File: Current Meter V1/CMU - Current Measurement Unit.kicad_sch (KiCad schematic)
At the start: 29 parts, among them J101 I2C OLED Display Connector, U101 MCP6002-xSN, U102 A1308xLHxx-1, U103 STM32L432KCUx

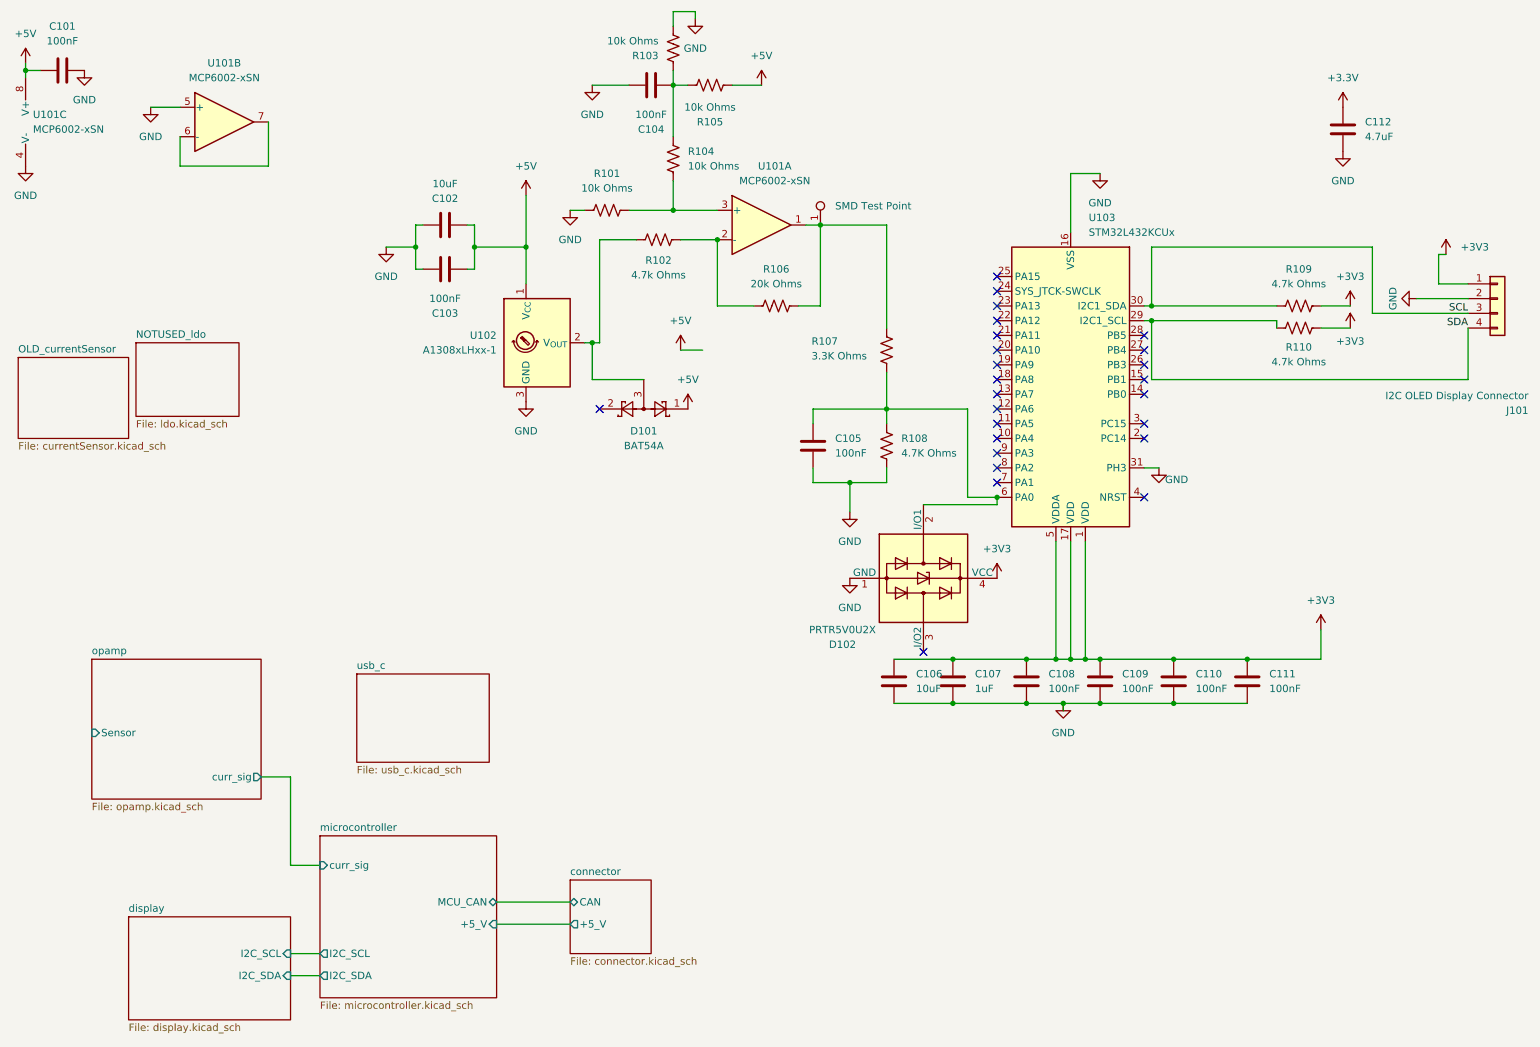
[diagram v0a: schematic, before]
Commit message: updated footprints
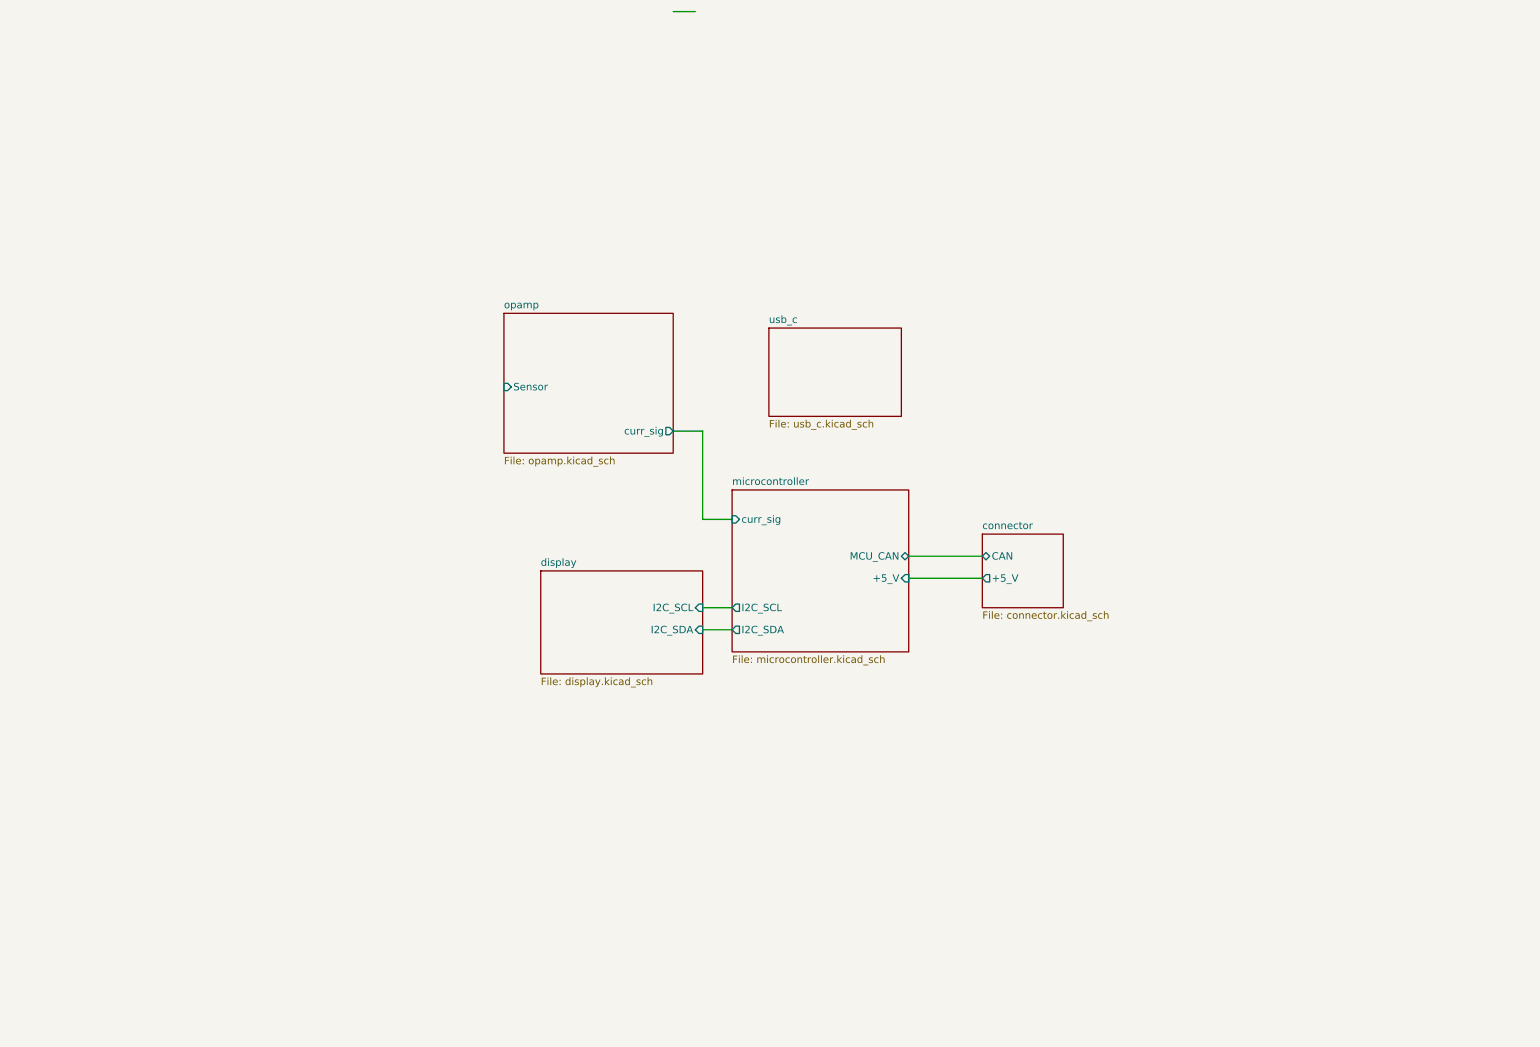
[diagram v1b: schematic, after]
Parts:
- removed C101, C103, C104, C105, C108, C109, C110, C111: 100nF, symbol Device:C
- removed C102, C106: 10uF, symbol Device:C
- removed C107: 1uF, symbol Device:C
- removed C112: 4.7uF, symbol Device:C
- removed D101: BAT54A, Package_TO_SOT_SMD:SOT-23, symbol Diode:BAT54A
- removed D102: PRTR5V0U2X, Package_TO_SOT_SMD:SOT-143, symbol Power_Protection:PRTR5V0U2X
- removed J101: I2C OLED Display Connector, symbol Connector_Generic:Conn_01x04
- removed R101, R103, R104, R105: 10k Ohms, symbol Device:R_US
- removed R102, R109, R110: 4.7k Ohms, symbol Device:R_US
- removed R106: 20k Ohms, symbol Device:R_US
- removed R107: 3.3K Ohms, symbol Device:R_US
- removed R108: 4.7K Ohms, symbol Device:R_US
- removed TP101: SMD Test Point, TestPoint:TestPoint_Keystone_5019_Miniature, symbol bfr_utilities:SMD_Test_Point
- removed U101: MCP6002-xSN, symbol Amplifier_Operational:MCP6002-xSN
- removed U102: A1308xLHxx-1, Package_TO_SOT_SMD:SOT-23W, symbol Sensor_Magnetic:A1308xLHxx-1
- removed U103: STM32L432KCUx, Package_DFN_QFN:QFN-32-1EP_5x5mm_P0.5mm_EP3.45x3.45mm, symbol MCU_ST_STM32L4:STM32L432KCUx
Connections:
- no-connect marks 25 -> 0
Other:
- removed sheet NOTUSED_ldo
- removed sheet OLD_currentSensor

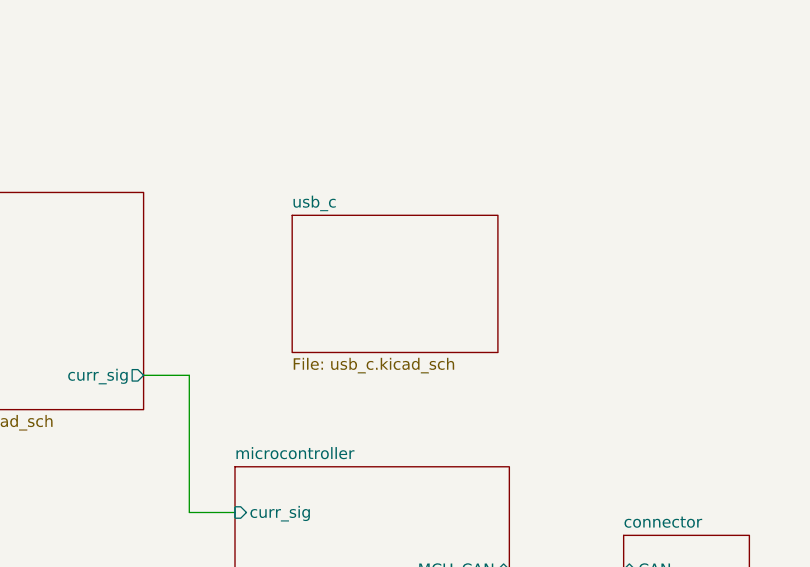
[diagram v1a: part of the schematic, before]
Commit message: footprints fully updated
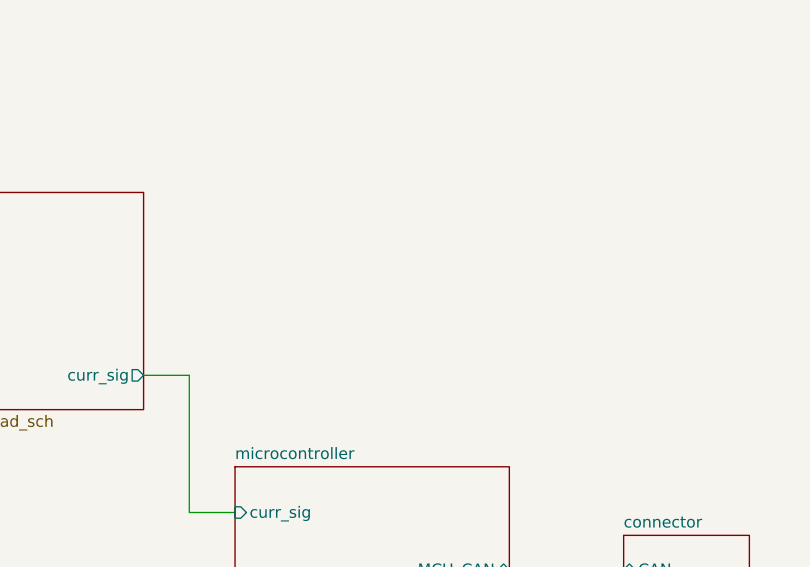
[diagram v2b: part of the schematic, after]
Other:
- removed sheet usb_c
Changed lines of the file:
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@@
-	)
-	(sheet
-		(at 147.32 69.85)
-		(size 22.86 15.24)
-		(exclude_from_sim no)
-		(in_bom yes)
-		(on_board yes)
-		(dnp no)
-		(fields_autoplaced yes)
-		(stroke
-			(width 0.1524)
-			(type solid)
-		)
-		(fill
-			(color 0 0 0 0.0000)
-		)
-		(property "Sheetname" "usb_c"
-			(at 147.32 69.1384 0)
-			(effects
-				(font
-					(size 1.27 1.27)
-				)
-				(justify left bottom)
-			)
-		)
-		(property "Sheetfile" "usb_c.kicad_sch"
-			(at 147.32 85.6746 0)
-			(effects
-				(font
-					(size 1.27 1.27)
-				)
-				(justify left top)
-			)
-		)
-		(instances
-			(project "CMU - Current Measurement Unit"
-				(path "/a2a38fd0-928e-4aba-88ec-c7bc808fdbf7"
-					(page "6")
-				)
-			)
-		)
 	)
 	(sheet

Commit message: buck converter
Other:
- added sheet buck (buck.kicad_sch)
- sheet connector ports: added +12_V; removed +5_V
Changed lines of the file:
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@@
 			)
 		)
-		(pin "+5_V" output
+		(pin "+12_V" output
 			(at 184.15 113.03 180)
 			(effects
@@
 				)
 			)
+		)
+	)
+	(sheet
+		(at 175.26 128.27)
+		(size 41.91 21.59)
+		(exclude_from_sim no)
+		(in_bom yes)
+		(on_board yes)
+		(dnp no)
+		(fields_autoplaced yes)
+		(stroke
+			(width 0.1524)
+			(type solid)
+		)
+		(fill
+			(color 0 0 0 0.0000)
+		)
+		(property "Sheetname" "buck"
+			(at 175.26 127.5584 0)
+			(effects
+				(font
+					(size 1.27 1.27)
+				)
+				(justify left bottom)
+			)
+		)
+		(property "Sheetfile" "buck.kicad_sch"
+			(at 175.26 150.4446 0)
+			(effects
+				(font
+					(size 1.27 1.27)
+				)
+				(justify left top)
+			)
+		)
+		(property "Field2" ""
+			(at 175.26 128.27 0)
+			(effects
+				(font
+					(size 1.27 1.27)
+				)
+			)
+		)
+		(pin "+5_V" output
+			(at 184.15 128.27 90)
+			(effects
+				(font
+					(size 1.27 1.27)
+				)
+				(justify right)
+			)
+		)
+		(pin "VIN" input
+			(at 217.17 142.24 0)
+			(effects
+				(font
+					(size 1.27 1.27)
+				)
+				(justify right)
+			)
+		)
+		(instances
+			(project "CMU - Current Measurement Unit"
+				(path "/a2a38fd0-928e-4aba-88ec-c7bc808fdbf7"
+					(page "6")
+				)
+			)

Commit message: layup updated
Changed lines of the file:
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@@
+	(wire
+		(pts
+			(xy 203.2 113.03) (xy 203.2 128.27)
+		)
+		(stroke
+			(width 0)
+			(type default)
+		)
+	)
 	(wire
 		(pts
@@
 	(wire
 		(pts
+			(xy 180.34 128.27) (xy 180.34 113.03)
+		)
+		(stroke
+			(width 0)
+			(type default)
+		)
+	)
+	(wire
+		(pts
+			(xy 198.12 113.03) (xy 203.2 113.03)
+		)
+		(stroke
+			(width 0)
+			(type default)
+		)
+	)
+	(wire
+		(pts
 			(xy 171.45 109.22) (xy 184.15 109.22)
 		)
@@
 	(wire
 		(pts
-			(xy 171.45 113.03) (xy 184.15 113.03)
+			(xy 171.45 113.03) (xy 180.34 113.03)
 		)
 		(stroke
@@
 		)
 		(pin "+12_V" output
-			(at 184.15 113.03 180)
-			(effects
-				(font
-					(size 1.27 1.27)
-				)
-				(justify left)
+			(at 198.12 113.03 0)
+			(effects
+				(font
+					(size 1.27 1.27)
+				)
+				(justify right)
 			)
 		)
@@
 		)
 		(pin "+5_V" output
-			(at 184.15 128.27 90)
+			(at 180.34 128.27 90)
 			(effects
 				(font
@@
 		)
 		(pin "VIN" input
-			(at 217.17 142.24 0)
-			(effects
-				(font
+			(at 203.2 128.27 90)
+			(effects
+				(font

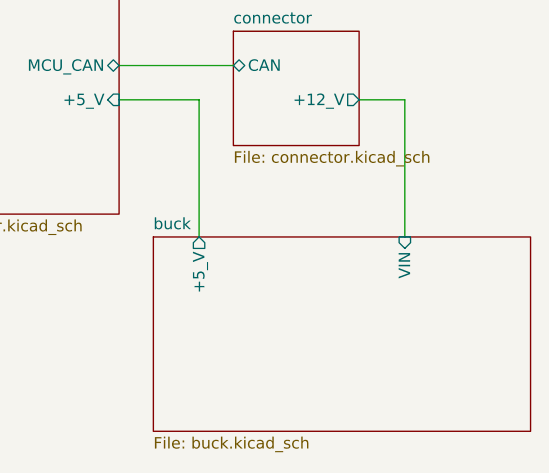
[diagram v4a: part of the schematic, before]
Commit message: updated layout
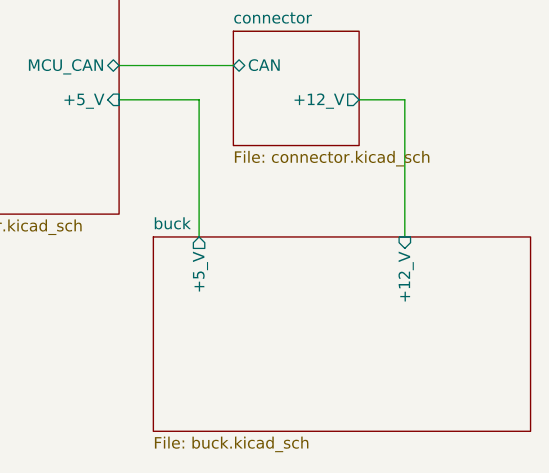
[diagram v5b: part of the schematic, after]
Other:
- sheet buck ports: added +12_V; removed VIN
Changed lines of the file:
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@@
 			)
 		)
-		(pin "VIN" input
+		(pin "+12_V" input
 			(at 203.2 128.27 90)
 			(effects

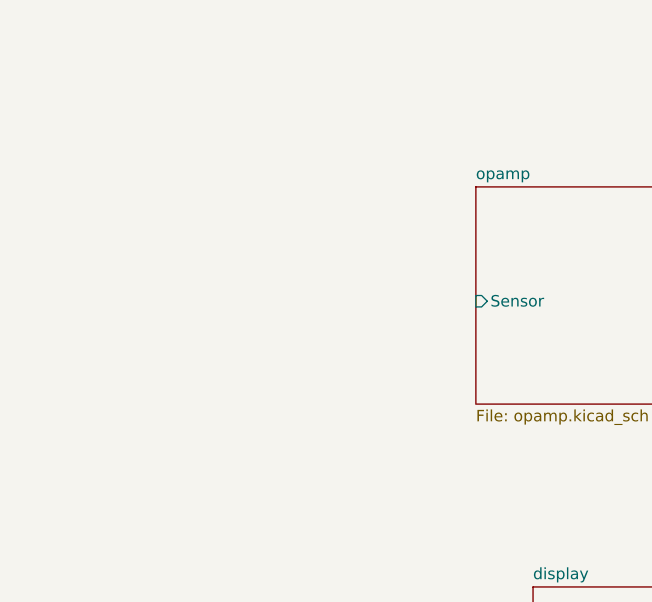
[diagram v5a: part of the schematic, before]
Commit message: added sensor connector, updated pcb layout
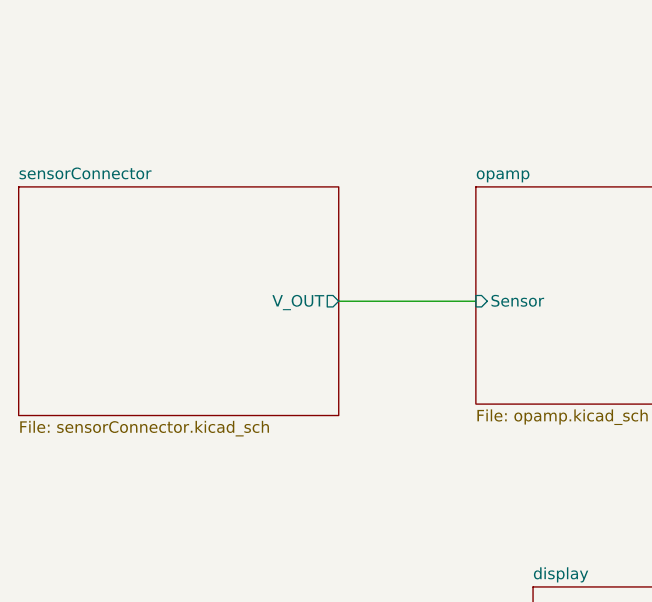
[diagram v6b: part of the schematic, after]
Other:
- added sheet sensorConnector (sensorConnector.kicad_sch)
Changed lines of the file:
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@@
+	(wire
+		(pts
+			(xy 86.36 80.01) (xy 101.6 80.01)
+		)
+		(stroke
+			(width 0)
+			(type default)
+		)
+	)
 	(wire
 		(pts
@@
 		)
 	)
+	(sheet
+		(at 50.8 67.31)
+		(size 35.56 25.4)
+		(exclude_from_sim no)
+		(in_bom yes)
+		(on_board yes)
+		(dnp no)
+		(fields_autoplaced yes)
+		(stroke
+			(width 0.1524)
+			(type solid)
+		)
+		(fill
+			(color 0 0 0 0.0000)
+		)
+		(property "Sheetname" "sensorConnector"
+			(at 50.8 66.5984 0)
+			(effects
+				(font
+					(size 1.27 1.27)
+				)
+				(justify left bottom)
+			)
+		)
+		(property "Sheetfile" "sensorConnector.kicad_sch"
+			(at 50.8 93.2946 0)
+			(effects
+				(font
+					(size 1.27 1.27)
+				)
+				(justify left top)
+			)
+		)
+		(property "Field2" ""
+			(at 50.8 67.31 0)
+			(effects
+				(font
+					(size 1.27 1.27)
+				)
+			)
+		)
+		(pin "V_OUT" output
+			(at 86.36 80.01 0)
+			(effects
+				(font
+					(size 1.27 1.27)
+				)
+				(justify right)
+			)
+		)
+		(instances
+			(project "CMU - Current Measurement Unit"
+				(path "/a2a38fd0-928e-4aba-88ec-c7bc808fdbf7"
+					(page "7")
+				)
+			)
+		)
+	)
